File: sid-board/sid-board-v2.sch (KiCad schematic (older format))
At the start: 45 parts, among them J1 ICM_CONN, J2 SID_CONN, J3 5V OUT, J4 3.3V OUT, J5 SPI/INT, Q1 BSS138, Q2 BSS138, Q3 BSS138, Q4 BSS138, U1 SC16IS752IPW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

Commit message: Working on SIDBOARD2 layout
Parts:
- renumbered J1 to ICM1, J2 to SID1
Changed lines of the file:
@@
 $EndComp
 $Comp
-L local_symbols:Conn_02x06_SAAB_SID_HPD J1
+L local_symbols:Conn_02x06_SAAB_SID_HPD ICM1
 U 1 1 5E210180
 P 1700 2600
-F 0 "J1" H 1700 3065 50  0000 C CNN
+F 0 "ICM1" H 1700 3065 50  0000 C CNN
 F 1 "ICM_CONN" H 1700 2974 50  0000 C CNN
 F 2 "sid-board:SAAB_SID_CONNECTOR_HEADER" H 1450 2600 50  0001 C CNN
@@
 $EndComp
 $Comp
-L local_symbols:Conn_02x06_SAAB_SID_HPD J2
+L local_symbols:Conn_02x06_SAAB_SID_HPD SID1
 U 1 1 5E211BEE
 P 1700 3600
-F 0 "J2" H 1700 4065 50  0000 C CNN
+F 0 "SID1" H 1700 4065 50  0000 C CNN
 F 1 "SID_CONN" H 1700 3974 50  0000 C CNN
 F 2 "sid-board:SAAB_SID_CONNECTOR_HEADER" H 1450 3600 50  0001 C CNN

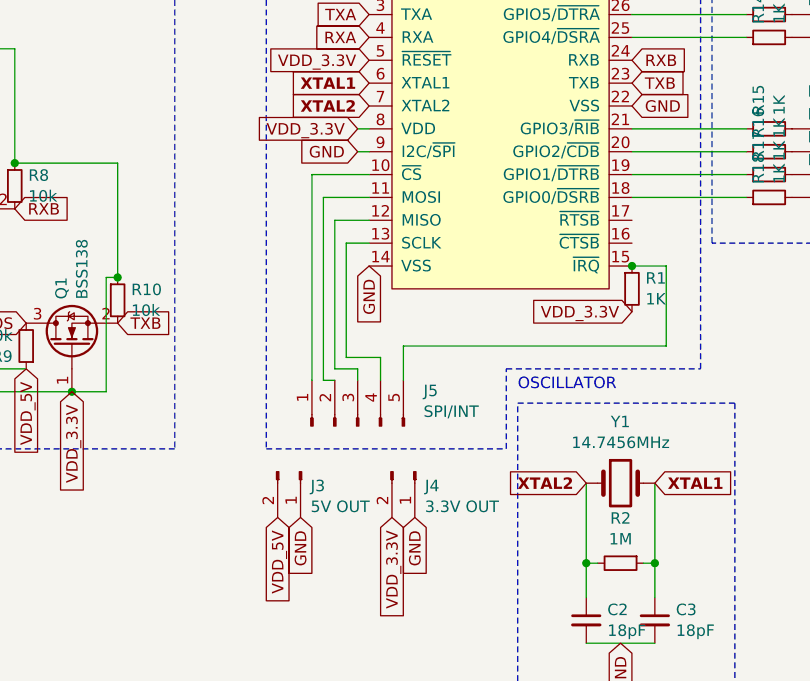
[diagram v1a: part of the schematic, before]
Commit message: Updated SPI layout and README.md
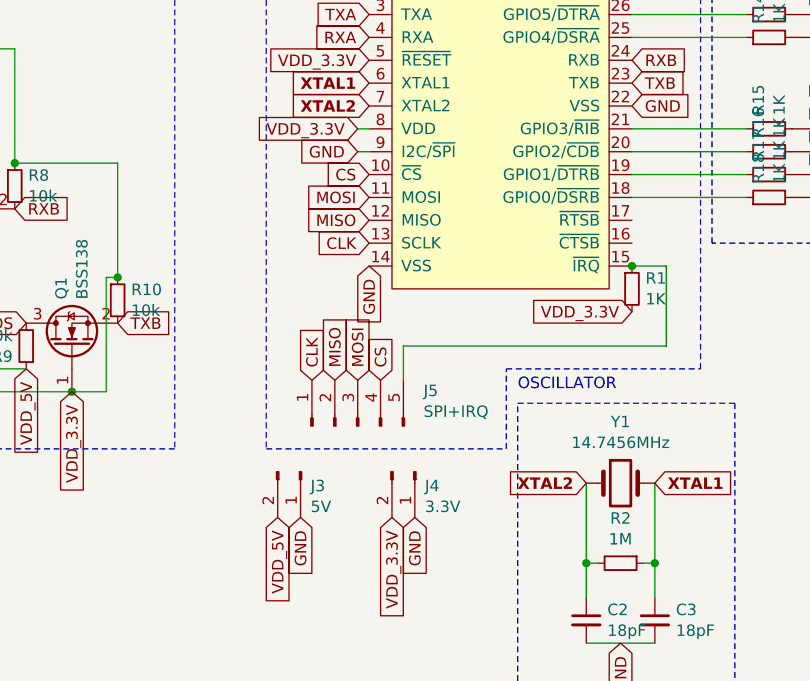
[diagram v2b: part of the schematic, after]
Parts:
- J3: value 5V OUT -> 5V
- J4: value 3.3V OUT -> 3.3V
- J5: value SPI/INT -> SPI+IRQ
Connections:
- net labels added: CLK, CS, MISO, MOSI
- wire segments 79 -> 66
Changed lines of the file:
@@
 Text GLabel 7500 2950 0    50   Input ~ 0
 VDD_3.3V
-Wire Wire Line
-	7550 3450 7450 3450
-Wire Wire Line
-	7550 3350 7400 3350
-Wire Wire Line
-	7550 3250 7350 3250
-Wire Wire Line
-	7550 3150 7300 3150
 $Comp
 L Connector:Conn_01x05_Male J5
@@
 P 7500 4250
 F 0 "J5" V 7654 3962 50  0000 R CNN
-F 1 "SPI/INT" V 7563 3962 50  0000 R CNN
+F 1 "SPI+IRQ" V 7563 3962 50  0000 R CNN
 F 2 "Connector_PinHeader_2.54mm:PinHeader_1x05_P2.54mm_Vertical" H 7500 4250 50  0001 C CNN
 F 3 "~" H 7500 4250 50  0001 C CNN
@@
 P 7250 4450
 F 0 "J3" V 7312 4494 50  0000 L CNN
-F 1 "5V OUT" V 7403 4494 50  0000 L CNN
+F 1 "5V" V 7403 4494 50  0000 L CNN
 F 2 "Connector_PinHeader_2.54mm:PinHeader_1x02_P2.54mm_Vertical" H 7250 4450 50  0001 C CNN
 F 3 "~" H 7250 4450 50  0001 C CNN
@@
 P 7750 4450
 F 0 "J4" V 7812 4494 50  0000 L CNN
-F 1 "3.3V OUT" V 7903 4494 50  0000 L CNN
+F 1 "3.3V" V 7903 4494 50  0000 L CNN
 F 2 "Connector_PinHeader_2.54mm:PinHeader_1x02_P2.54mm_Vertical" H 7750 4450 50  0001 C CNN
 F 3 "~" H 7750 4450 50  0001 C CNN
@@
 Wire Wire Line
 	3400 5250 3400 4950
-Wire Wire Line
-	7300 3150 7300 4050
-Wire Wire Line
-	7350 4050 7400 4050
-Wire Wire Line
-	7350 3250 7350 4050
-Wire Wire Line
-	7400 4000 7500 4000
-Wire Wire Line
-	7500 4000 7500 4050
-Wire Wire Line
-	7400 3350 7400 4000
-Wire Wire Line
-	7450 3950 7600 3950
-Wire Wire Line
-	7600 3950 7600 4050
-Wire Wire Line
-	7450 3450 7450 3950
 Wire Wire Line
 	7700 4050 7700 3900
@@
 Text Notes 9050 2000 0    50   ~ 0
 GPIO LED OUTPUT
+Text GLabel 7550 3450 0    50   Input ~ 0
+CLK
+Text GLabel 7550 3350 0    50   Input ~ 0
+MISO
+Text GLabel 7550 3250 0    50   Input ~ 0
+MOSI
+Text GLabel 7550 3150 0    50   Input ~ 0
+CS
+Text GLabel 7300 4050 1    50   Input ~ 0
+CLK
+Text GLabel 7400 4050 1    50   Input ~ 0
+MISO
+Text GLabel 7500 4050 1    50   Input ~ 0
+MOSI
+Text GLabel 7600 4050 1    50   Input ~ 0
+CS
 $EndSCHEMATC

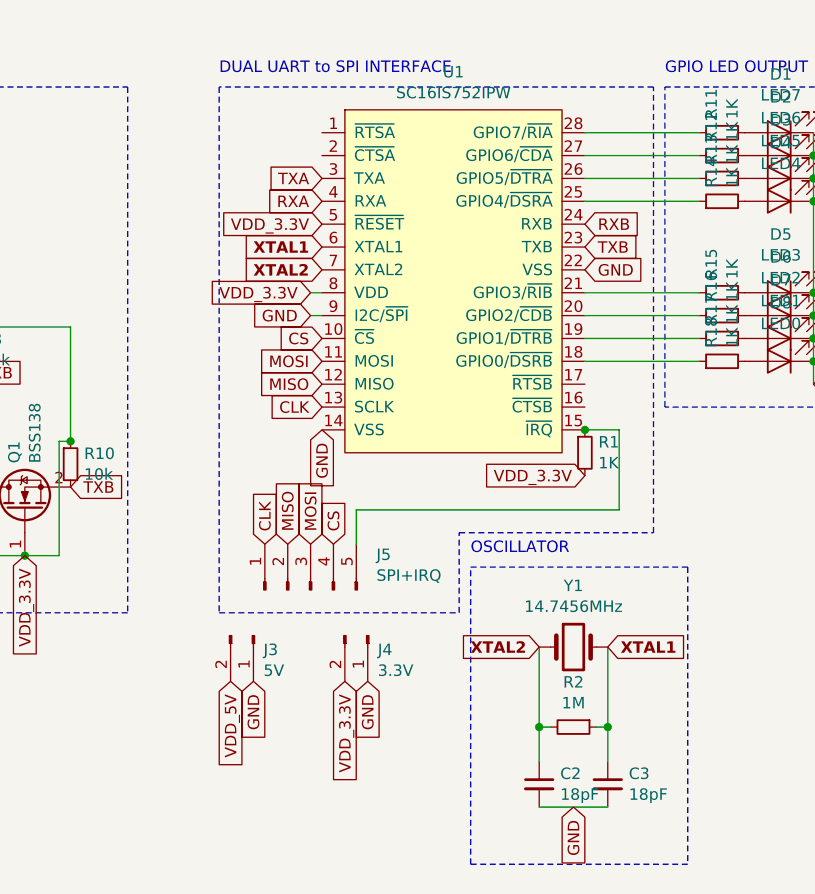
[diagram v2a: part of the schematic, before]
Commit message: Working on routing of sidboard v2.
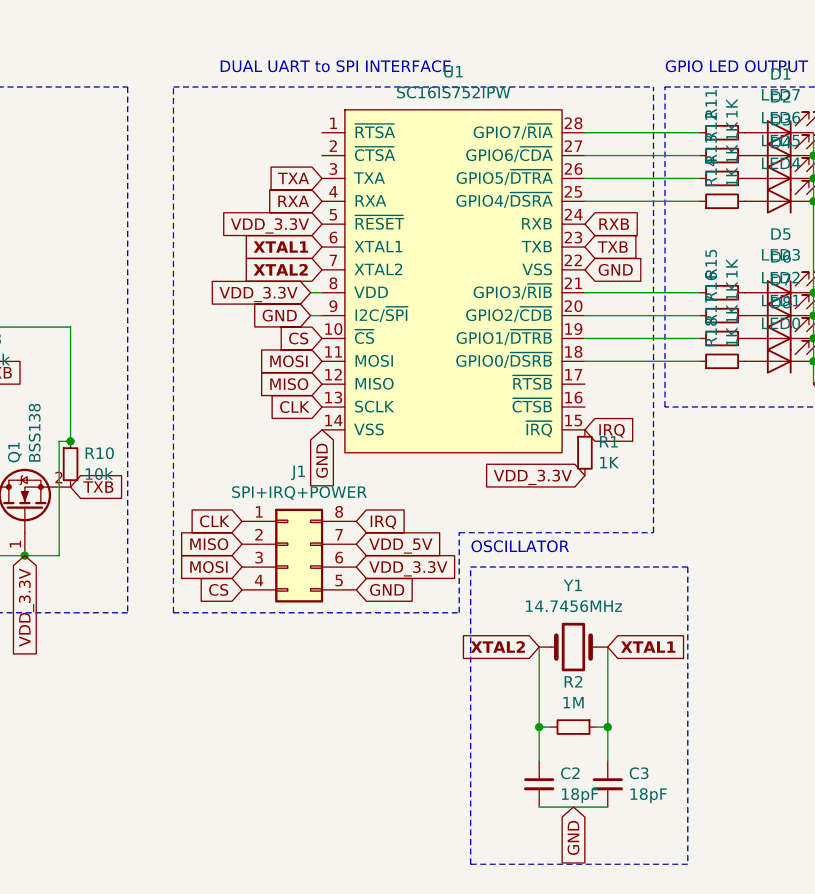
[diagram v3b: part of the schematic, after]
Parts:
- removed J3: 5V, Connector_PinHeader_2.54mm:PinHeader_1x02_P2.54mm_Vertical, symbol Connector:Conn_01x02_Male
- removed J4: 3.3V, Connector_PinHeader_2.54mm:PinHeader_1x02_P2.54mm_Vertical, symbol Connector:Conn_01x02_Male
- removed J5: SPI+IRQ, Connector_PinHeader_2.54mm:PinHeader_1x05_P2.54mm_Vertical, symbol Connector:Conn_01x05_Male
- added J1: SPI+IRQ+POWER, Connector_PinSocket_2.54mm:PinSocket_2x04_P2.54mm_Vertical, symbol Connector_Generic:Conn_02x04_Counter_Clockwise
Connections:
- net labels added: IRQ
- wire segments 66 -> 62
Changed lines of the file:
@@
 EESchema Schematic File Version 4
+LIBS:sid-board-v2-cache
 EELAYER 30 0
 EELAYER END
@@
 Wire Wire Line
 	7500 3050 7550 3050
-Text GLabel 7150 4650 3    50   Input ~ 0
+Text GLabel 7700 4050 2    50   Input ~ 0
 VDD_5V
-Text GLabel 7250 4650 3    50   Input ~ 0
-GND
-Text GLabel 7750 4650 3    50   Input ~ 0
-GND
-Text GLabel 7650 4650 3    50   Input ~ 0
+Text GLabel 7700 4250 2    50   Input ~ 0
+GND
+Text GLabel 7700 4150 2    50   Input ~ 0
 VDD_3.3V
 Text GLabel 7500 3050 0    50   Input ~ 0
@@
 Text GLabel 7500 2950 0    50   Input ~ 0
 VDD_3.3V
-$Comp
-L Connector:Conn_01x05_Male J5
-U 1 1 5E308950
-P 7500 4250
-F 0 "J5" V 7654 3962 50  0000 R CNN
-F 1 "SPI+IRQ" V 7563 3962 50  0000 R CNN
-F 2 "Connector_PinHeader_2.54mm:PinHeader_1x05_P2.54mm_Vertical" H 7500 4250 50  0001 C CNN
-F 3 "~" H 7500 4250 50  0001 C CNN
-	1    7500 4250
-	0    -1   -1   0
-$EndComp
-$Comp
-L Connector:Conn_01x02_Male J3
-U 1 1 5E30F0FD
-P 7250 4450
-F 0 "J3" V 7312 4494 50  0000 L CNN
-F 1 "5V" V 7403 4494 50  0000 L CNN
-F 2 "Connector_PinHeader_2.54mm:PinHeader_1x02_P2.54mm_Vertical" H 7250 4450 50  0001 C CNN
-F 3 "~" H 7250 4450 50  0001 C CNN
-	1    7250 4450
-	0    1    1    0
-$EndComp
-$Comp
-L Connector:Conn_01x02_Male J4
-U 1 1 5E310D87
-P 7750 4450
-F 0 "J4" V 7812 4494 50  0000 L CNN
-F 1 "3.3V" V 7903 4494 50  0000 L CNN
-F 2 "Connector_PinHeader_2.54mm:PinHeader_1x02_P2.54mm_Vertical" H 7750 4450 50  0001 C CNN
-F 3 "~" H 7750 4450 50  0001 C CNN
-	1    7750 4450
-	0    1    1    0
-$EndComp
 $Comp
 L Device:R_Small R1
@@
 Wire Wire Line
 	3400 5250 3400 4950
-Wire Wire Line
-	7700 4050 7700 3900
-Wire Wire Line
-	7700 3900 8850 3900
-Wire Wire Line
-	8850 3900 8850 3550
-Wire Wire Line
-	8850 3550 8700 3550
-Connection ~ 8700 3550
 Text GLabel 7550 2650 0    50   Input ~ 0
 VDD_3.3V
@@
 GND
 Wire Notes Line
-	7100 2050 7100 4350
-Wire Notes Line
-	7100 4350 8150 4350
-Wire Notes Line
 	8150 4350 8150 4000
 Wire Notes Line
@@
 Wire Notes Line
 	9000 4000 9000 2050
-Wire Notes Line
-	9000 2050 7100 2050
 Text Notes 7100 2000 0    50   ~ 0
 DUAL UART to SPI INTERFACE
@@
 Text GLabel 7550 3150 0    50   Input ~ 0
 CS
-Text GLabel 7300 4050 1    50   Input ~ 0
+Text GLabel 7200 3950 0    50   Input ~ 0
 CLK
-Text GLabel 7400 4050 1    50   Input ~ 0
+Text GLabel 7200 4050 0    50   Input ~ 0
 MISO
-Text GLabel 7500 4050 1    50   Input ~ 0
+Text GLabel 7200 4150 0    50   Input ~ 0
 MOSI
-Text GLabel 7600 4050 1    50   Input ~ 0
+Text GLabel 7200 4250 0    50   Input ~ 0
 CS
+$Comp
+L Connector_Generic:Conn_02x04_Counter_Clockwise J1
+U 1 1 5E4709DB
+P 7400 4050
+F 0 "J1" H 7450 4367 50  0000 C CNN
+F 1 "SPI+IRQ+POWER" H 7450 4276 50  0000 C CNN
+F 2 "Connector_PinSocket_2.54mm:PinSocket_2x04_P2.54mm_Vertical" H 7400 4050 50  0001 C CNN
+F 3 "~" H 7400 4050 50  0001 C CNN
+	1    7400 4050
+	1    0    0    -1
+$EndComp
+Text GLabel 8700 3550 2    50   Input ~ 0
+IRQ
+Text GLabel 7700 3950 2    50   Input ~ 0
+IRQ
+Wire Notes Line
+	6900 4350 6900 2050
+Wire Notes Line
+	6900 4350 8150 4350
+Wire Notes Line
+	6900 2050 9000 2050
 $EndSCHEMATC

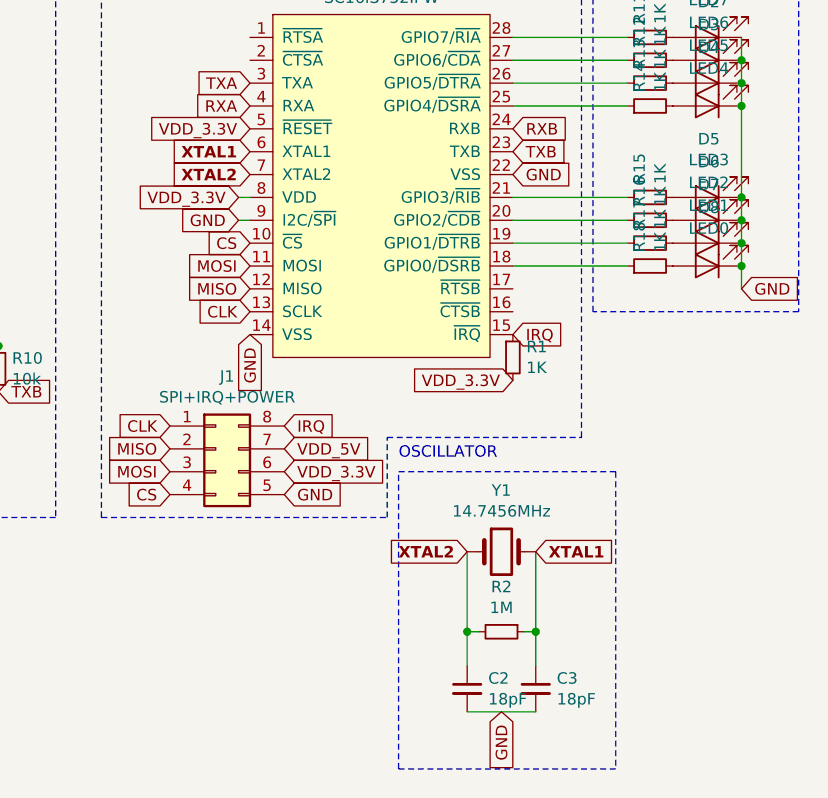
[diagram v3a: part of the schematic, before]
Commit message: Added new custom footprint for crystal oscillator module, replacing the old crystal module
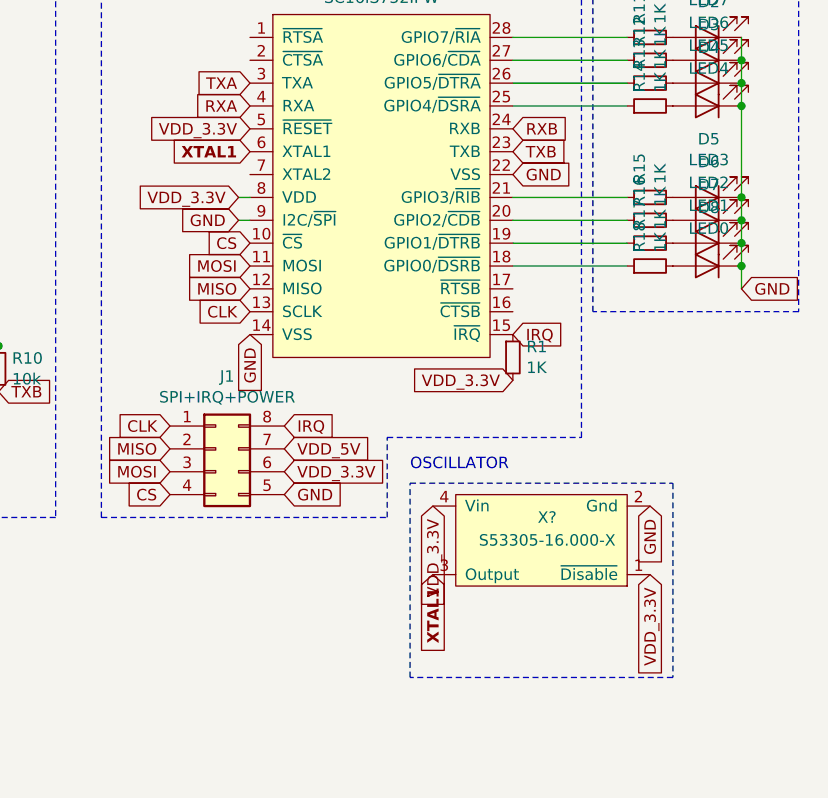
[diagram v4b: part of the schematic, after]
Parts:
- removed C2, C3: 18pF, Capacitor_SMD:C_0805_2012Metric_Pad1.15x1.40mm_HandSolder, symbol Device:C_Small
- removed R2: 1M, Resistor_SMD:R_0805_2012Metric_Pad1.15x1.40mm_HandSolder, symbol Device:R_Small
- removed Y1: 14.7456MHz, sid-board:Euroquarts 14.7456MHz Crystal ±30ppm SMD 2-Pin 12.4 x 4.5 x 4.2mm, symbol Device:Crystal
- added X?: S53305-16.000-X, sid-board:S53305-16.000-X, symbol local_symbols:S53305-16.000-X
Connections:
- net labels removed: XTAL2
- wire segments 62 -> 55
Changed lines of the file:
@@
 EESchema Schematic File Version 4
-LIBS:sid-board-v2-cache
 EELAYER 30 0
 EELAYER END
@@
 Text GLabel 7550 2750 0    50   Input ~ 10
 XTAL1
-Text GLabel 7550 2850 0    50   Input ~ 10
-XTAL2
 $Comp
 L Device:C_Small C4
@@
 Text Notes 7100 2000 0    50   ~ 0
 DUAL UART to SPI INTERFACE
-Text Notes 8200 4100 0    50   ~ 0
+Text Notes 8250 4150 0    50   ~ 0
 OSCILLATOR
-Wire Notes Line
-	8200 5450 8200 4150
-Wire Notes Line
-	9150 5450 8200 5450
-Wire Notes Line
-	9150 4150 9150 5450
-Wire Notes Line
-	8200 4150 9150 4150
-Text GLabel 8500 4500 0    50   Input ~ 10
-XTAL2
-Text GLabel 8800 4500 2    50   Input ~ 10
+Text GLabel 8350 4600 3    50   Input ~ 10
 XTAL1
-Text GLabel 8650 5200 3    50   Input ~ 0
-GND
-Connection ~ 8800 4850
-Wire Wire Line
-	8800 4850 8800 5000
-Wire Wire Line
-	8500 5200 8800 5200
-Wire Wire Line
-	8800 4850 8750 4850
-Wire Wire Line
-	8800 4500 8800 4850
-Connection ~ 8500 4850
-Wire Wire Line
-	8500 4850 8500 5000
-Wire Wire Line
-	8500 4850 8550 4850
-Wire Wire Line
-	8500 4500 8500 4850
-$Comp
-L Device:C_Small C3
-U 1 1 5E2BA581
-P 8800 5100
-F 0 "C3" H 8892 5146 50  0000 L CNN
-F 1 "18pF" H 8892 5055 50  0000 L CNN
-F 2 "Capacitor_SMD:C_0805_2012Metric_Pad1.15x1.40mm_HandSolder" H 8800 5100 50  0001 C CNN
-F 3 "~" H 8800 5100 50  0001 C CNN
-	1    8800 5100
-	1    0    0    -1
-$EndComp
-$Comp
-L Device:C_Small C2
-U 1 1 5E2B9259
-P 8500 5100
-F 0 "C2" H 8592 5146 50  0000 L CNN
-F 1 "18pF" H 8592 5055 50  0000 L CNN
-F 2 "Capacitor_SMD:C_0805_2012Metric_Pad1.15x1.40mm_HandSolder" H 8500 5100 50  0001 C CNN
-F 3 "~" H 8500 5100 50  0001 C CNN
-	1    8500 5100
-	1    0    0    -1
-$EndComp
-$Comp
-L Device:R_Small R2
-U 1 1 5E2B87B7
-P 8650 4850
-F 0 "R2" V 8454 4850 50  0000 C CNN
-F 1 "1M" V 8545 4850 50  0000 C CNN
-F 2 "Resistor_SMD:R_0805_2012Metric_Pad1.15x1.40mm_HandSolder" H 8650 4850 50  0001 C CNN
-F 3 "~" H 8650 4850 50  0001 C CNN
-	1    8650 4850
-	0    1    1    0
-$EndComp
-$Comp
-L Device:Crystal Y1
-U 1 1 5E2B8361
-P 8650 4500
-F 0 "Y1" H 8650 4768 50  0000 C CNN
-F 1 "14.7456MHz" H 8650 4677 50  0000 C CNN
-F 2 "sid-board:Euroquarts 14.7456MHz Crystal ±30ppm SMD 2-Pin 12.4 x 4.5 x 4.2mm" H 8650 4500 50  0001 C CNN
-F 3 "~" H 8650 4500 50  0001 C CNN
-	1    8650 4500
-	1    0    0    -1
-$EndComp
+Text GLabel 9300 4300 3    50   Input ~ 0
+GND
 $Comp
 L Transistor_FET:BSS138 Q1
@@
 Wire Notes Line
 	6900 2050 9000 2050
+$Comp
+L local_symbols:S53305-16.000-X X?
+U 1 1 5E7AFB1C
+P 8850 4500
+F 0 "X?" H 8850 4350 50  0000 C CNN
+F 1 "S53305-16.000-X" H 8850 4450 50  0000 C CNN
+F 2 "sid-board:S53305-16.000-X" H 8850 4500 50  0001 C CNN
+F 3 "" H 8850 4500 50  0001 C CNN
+	1    8850 4500
+	-1   0    0    1
+$EndComp
+Text GLabel 8350 4300 3    50   Input ~ 0
+VDD_3.3V
+Text GLabel 9300 4600 3    50   Input ~ 0
+VDD_3.3V
+Wire Notes Line
+	8250 4200 9400 4200
+Wire Notes Line
+	9400 4200 9400 5050
+Wire Notes Line
+	9400 5050 8250 5050
+Wire Notes Line
+	8250 5050 8250 4200
 $EndSCHEMATC

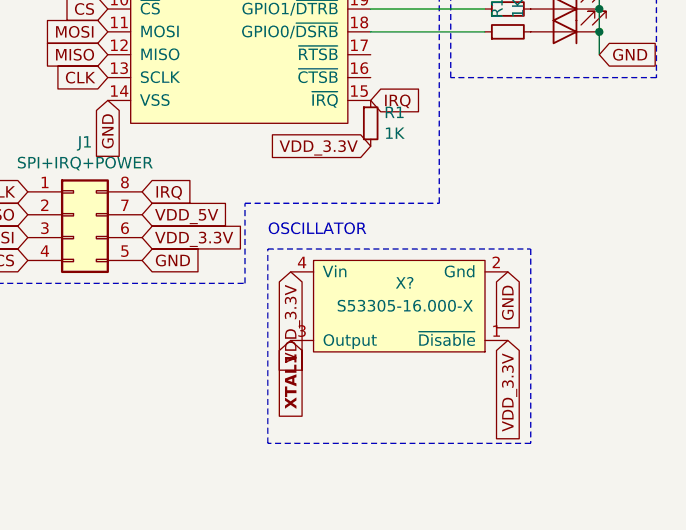
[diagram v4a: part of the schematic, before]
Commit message: Replaced crystal with oscillator module on PCB
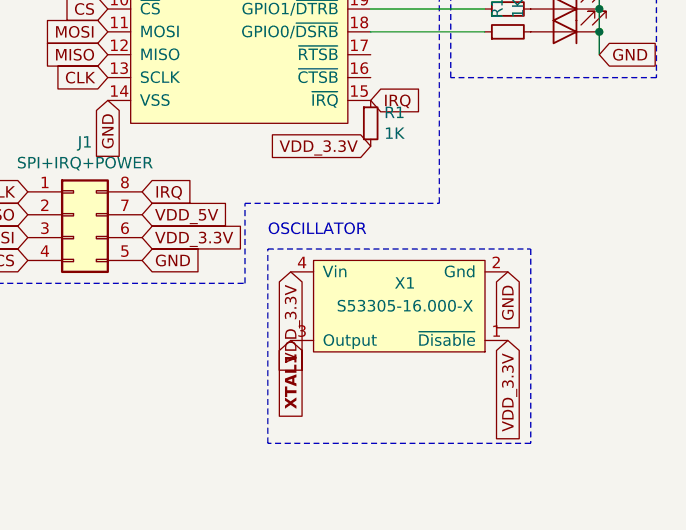
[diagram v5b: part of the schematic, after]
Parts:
- gave numbers to parts that had none: 1
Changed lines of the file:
@@
 	6900 2050 9000 2050
 $Comp
-L local_symbols:S53305-16.000-X X?
+L local_symbols:S53305-16.000-X X1
 U 1 1 5E7AFB1C
 P 8850 4500
-F 0 "X?" H 8850 4350 50  0000 C CNN
+F 0 "X1" H 8850 4350 50  0000 C CNN
 F 1 "S53305-16.000-X" H 8850 4450 50  0000 C CNN
 F 2 "sid-board:S53305-16.000-X" H 8850 4500 50  0001 C CNN
